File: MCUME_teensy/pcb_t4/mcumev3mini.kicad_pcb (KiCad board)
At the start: 2 copper layers, 46 x 26.3 mm, 0 parts

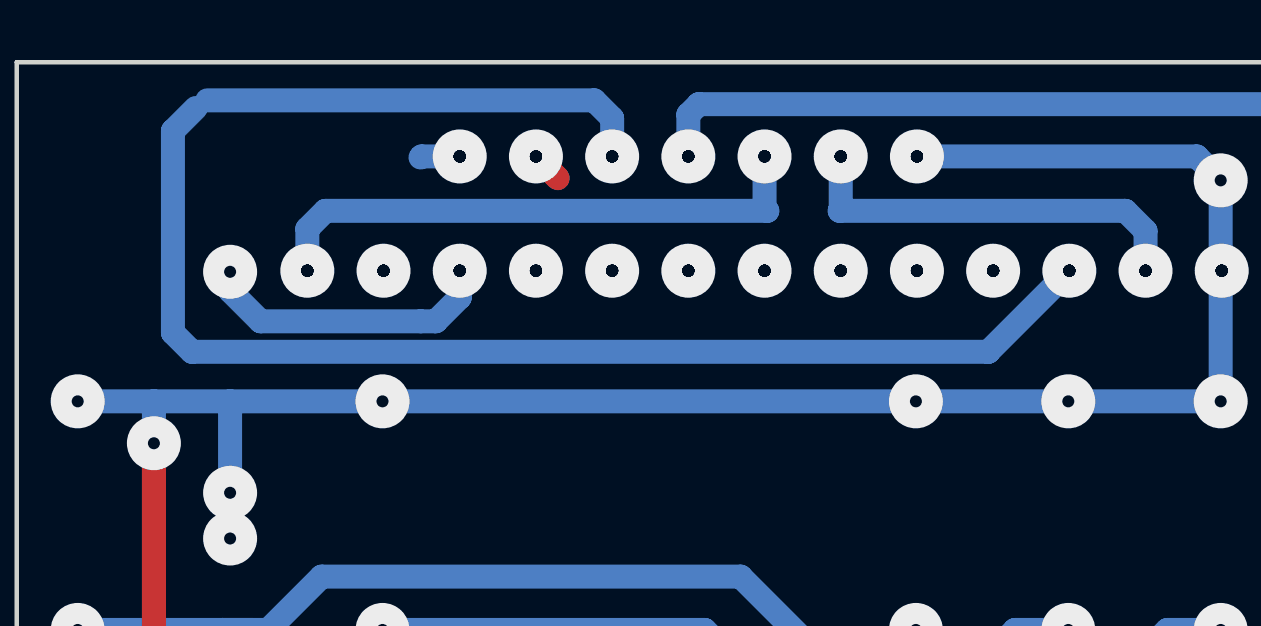
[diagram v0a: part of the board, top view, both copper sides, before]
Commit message: add support for 320x240 st7789 display
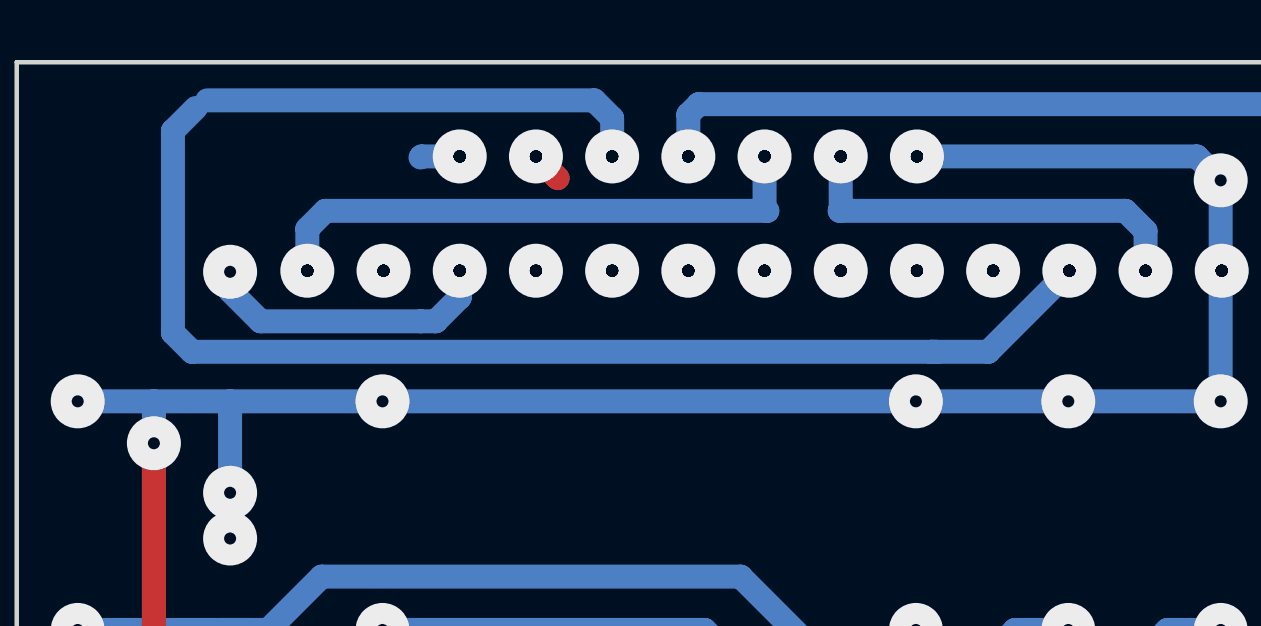
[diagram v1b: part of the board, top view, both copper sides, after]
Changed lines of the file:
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@@
     (thickness 1.6)
     (drawings 4)
-    (tracks 343)
+    (tracks 344)
     (zones 0)
     (modules 0)
@@
   (segment (start 158.784583 26.254417) (end 157.988 27.051) (width 0.8) (layer B.Cu) (net 0))
   (segment (start 158.784583 25.364137) (end 158.784583 26.254417) (width 0.8) (layer B.Cu) (net 0))
-  (segment (start 176.403 28.06572) (end 176.403 28.067) (width 0.8) (layer B.Cu) (net 0))
-  (segment (start 179.104583 25.364137) (end 176.403 28.06572) (width 0.8) (layer B.Cu) (net 0))
   (segment (start 149.987 19.939) (end 149.225 20.701) (width 0.8) (layer B.Cu) (net 0))
   (segment (start 149.225 27.432) (end 149.86 28.067) (width 0.8) (layer B.Cu) (net 0))
   (segment (start 149.225 20.701) (end 149.225 27.432) (width 0.8) (layer B.Cu) (net 0))
-  (segment (start 176.403 28.067) (end 149.86 28.067) (width 0.8) (layer B.Cu) (net 0))
   (segment (start 184.15 29.718) (end 151.13 29.718) (width 0.8) (layer B.Cu) (net 0))
   (segment (start 161.324583 21.554137) (end 162.052 22.281554) (width 0.8) (layer F.Cu) (net 0))
@@
   (segment (start 112.915183 36.770625) (end 94.674375 36.770625) (width 0.8) (layer B.Cu) (net 0))
   (segment (start 112.915183 39.310625) (end 94.801375 39.310625) (width 0.8) (layer B.Cu) (net 0))
+  (segment (start 174.710248 28.067) (end 174.498 28.067) (width 0.8) (layer B.Cu) (net 0))
+  (segment (start 174.498 28.067) (end 149.86 28.067) (width 0.8) (layer B.Cu) (net 0))
+  (segment (start 176.40172 28.067) (end 179.104583 25.364137) (width 0.8) (layer B.Cu) (net 0))
+  (segment (start 174.498 28.067) (end 176.40172 28.067) (width 0.8) (layer B.Cu) (net 0))
 )
